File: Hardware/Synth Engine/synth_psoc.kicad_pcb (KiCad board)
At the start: 2 copper layers, 230 parts, among them J1 Barrel_Jack, J10 Conn_01x13, J11 Conn_01x13, J12 Conn_01x06, J13 Conn_01x05, J14 Conn_01x05, J15 Conn_01x05, J16 Conn_01x05, J2 Audio-Jack-2_Switch, J3 SWD_programming, J4 Conn_01x08, J5 Conn_01x02, J6 Conn_01x03, J7 Capsense_buttons, J8 Conn_01x13, J9 Conn_01x13, Q1 MMBT3904-TP, Q2 MMBT3904-TP, Q3 MMBT3904-TP, Q4 MMBT3904-TP, Q5 MMBFJ177, Q6 MMBFJ177, Q7 MMBFJ177, Q8 MMBFJ177, U1 TL074, U2 TL074, U3 TL074, U4 TL074, U5 TL074, U6 CY8C4246AZI-L445, U7 V7805-1000, U8 PT2399, Y1 Crystal

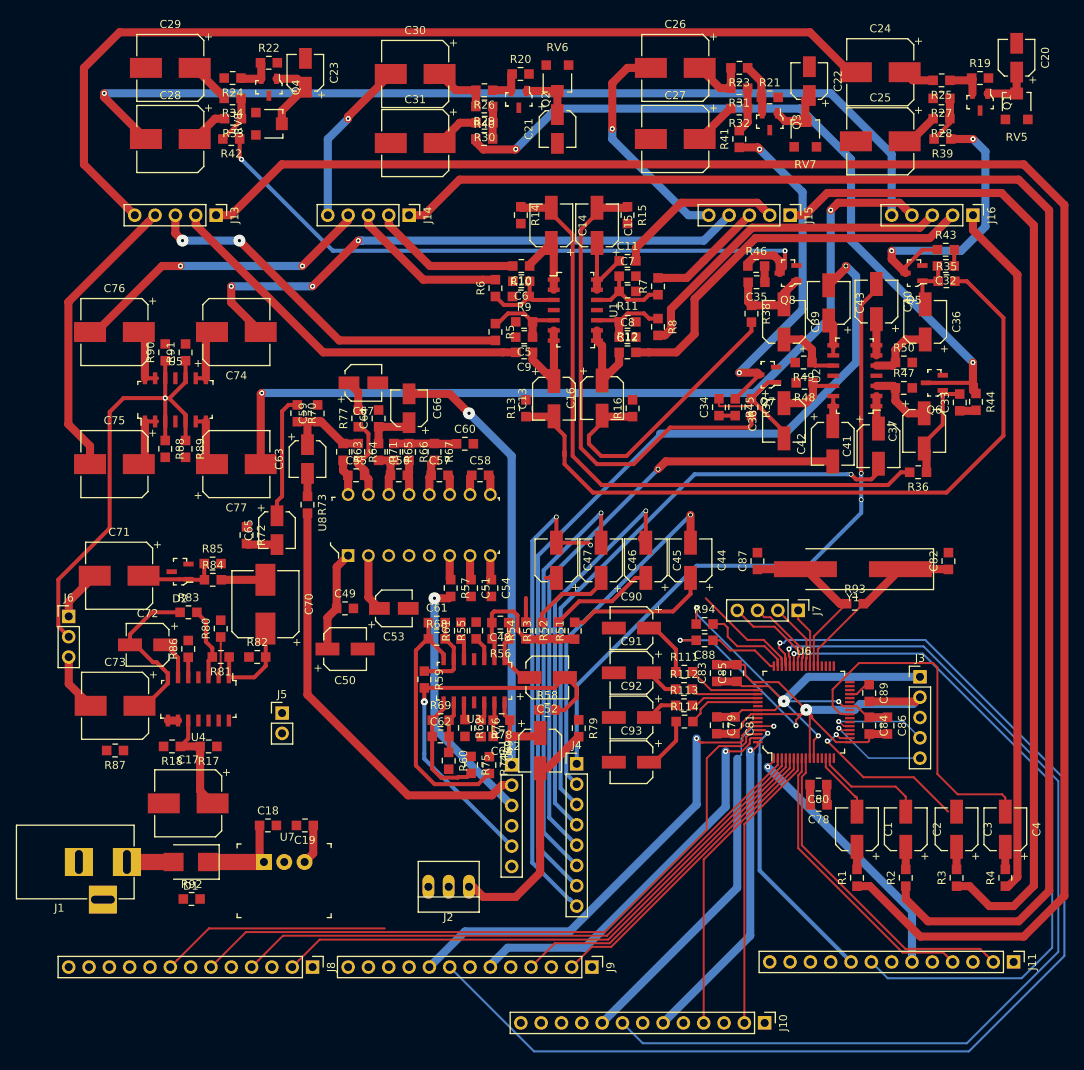
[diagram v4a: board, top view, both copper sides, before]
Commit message: finish routing connectors and start routing +15V
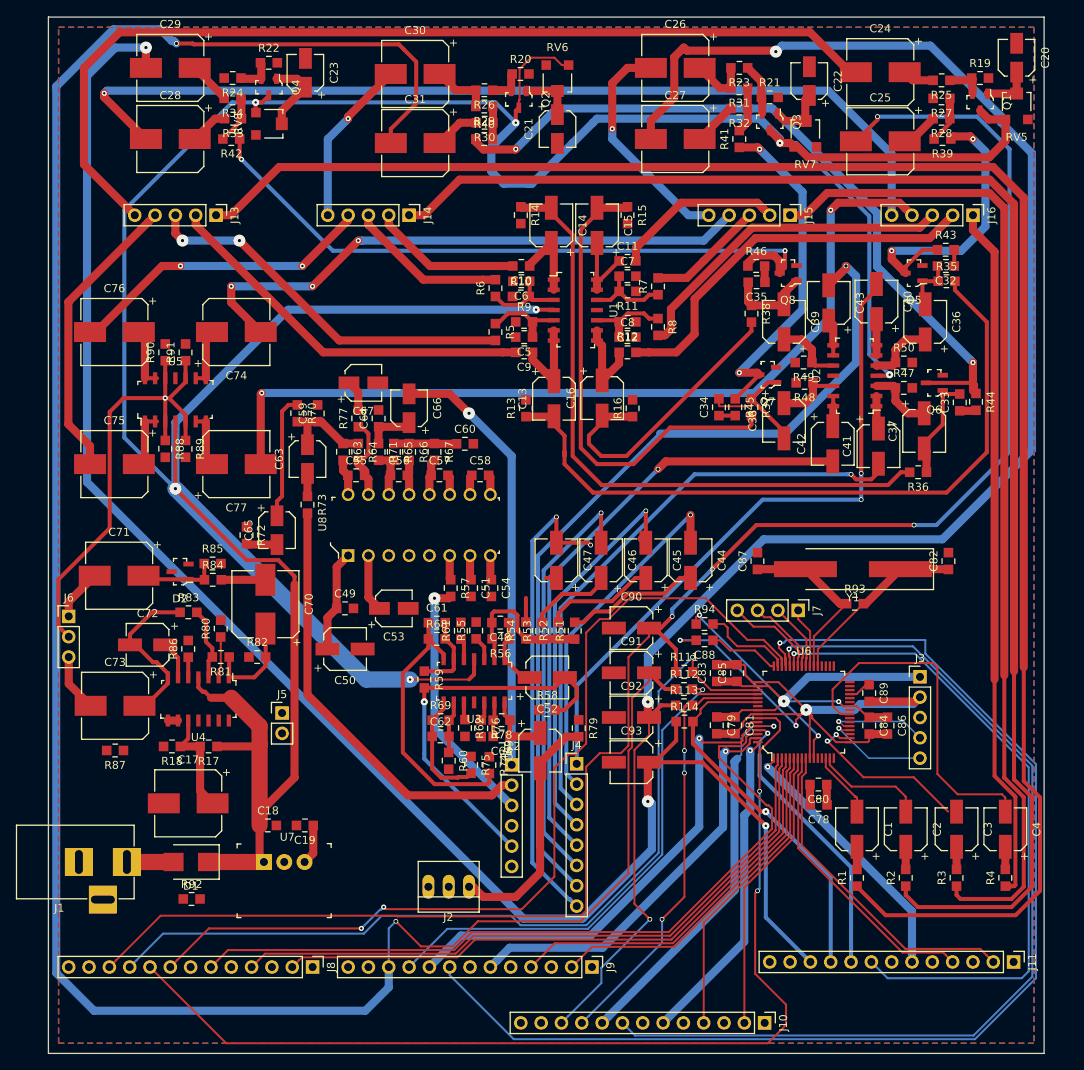
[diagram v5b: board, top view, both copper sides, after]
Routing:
- net +15V: track 11.8 -> 447.2 mm, vias 0 -> 7
- net /Microcontroller/envelope_pwm_2: track 4.16 -> 289.7 mm, vias 0 -> 2
- net /Microcontroller/envelope_pwm_1: track 7.26 -> 224.9 mm, vias 0 -> 4
- net /Microcontroller/envelope_pwm_3: track 3.95 -> 215.0 mm, vias 0 -> 3
- net /Microcontroller/envelope_pwm_4: track 6.89 -> 214.4 mm, vias 0 -> 3
- net /Connectors/osc1_quant: track 0.00 -> 128.1 mm, vias 0 -> 2
- net /Connectors/envelope_pwm_bypass_in_1: track 9.09 -> 110.2 mm, vias 0 -> 1
- net /Connectors/osc1_repeat: track 42.4 -> 115.9 mm, vias 0 -> 2
- net /Connectors/envelope_pwm_bypass_in_2: track 8.44 -> 69.9 mm, vias 0 -> 1
- net /Connectors/envelope_pwm_bypass_in_3: track 8.55 -> 54.5 mm, vias 0 -> 3
- net /Connectors/envelope_pwm_bypass_in_4: track 9.45 -> 47.0 mm, vias 0 -> 1
- net /Connectors/osc1_speed: track 86.0 -> 96.4 mm
- net /Connectors/freq_in_1: track 227.8 -> 218.2 mm
- net /Connectors/freq_in_2: track 190.8 -> 183.5 mm
- net /Connectors/osc2_pwm_wiper: track 43.3 -> 48.0 mm
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- added copper zone on B.Cu, net GND
- added copper zone on F.Cu, net GND
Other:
- board outline added: 124.5 x 129.5 mm

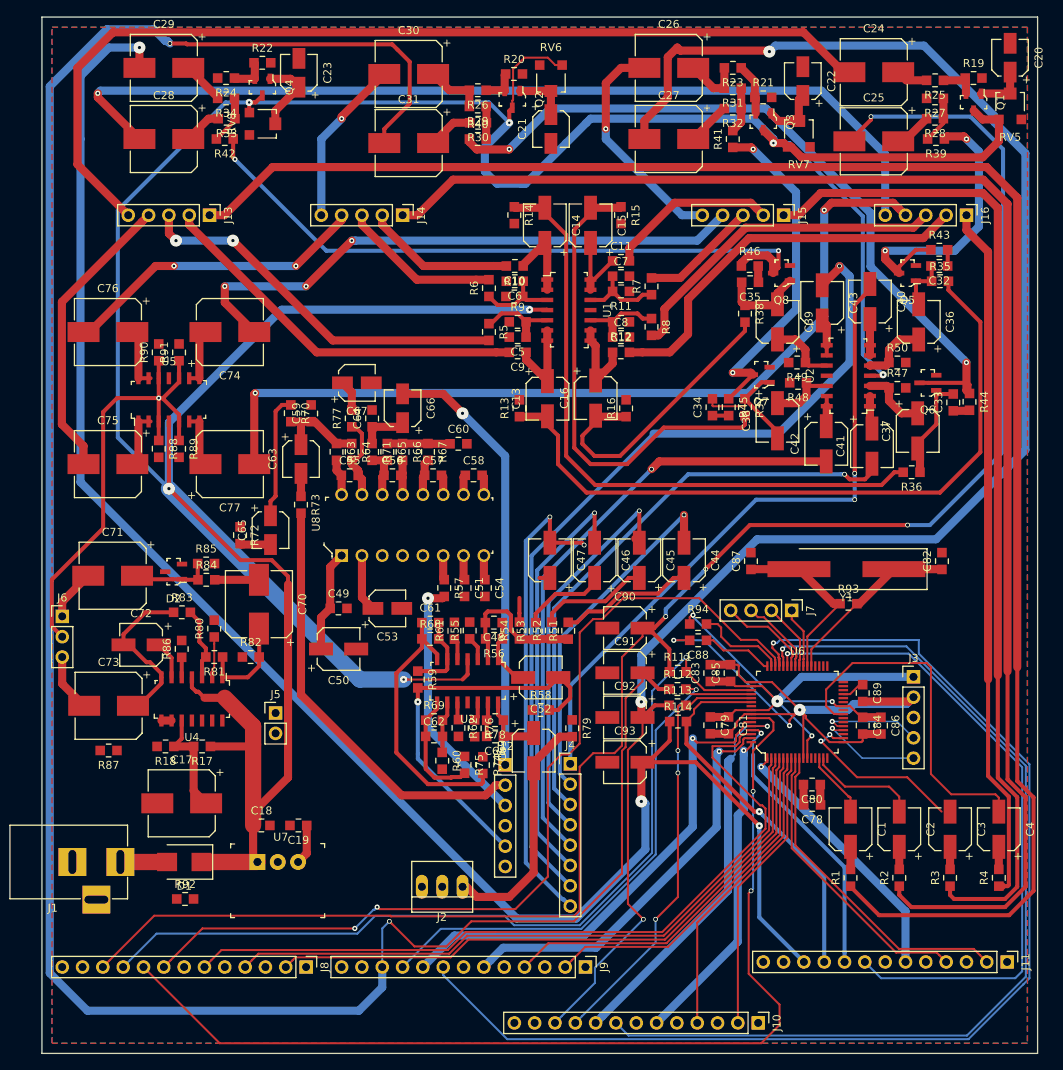
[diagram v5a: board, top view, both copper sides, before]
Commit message: PCBv2 release candidate. Passes DRC.
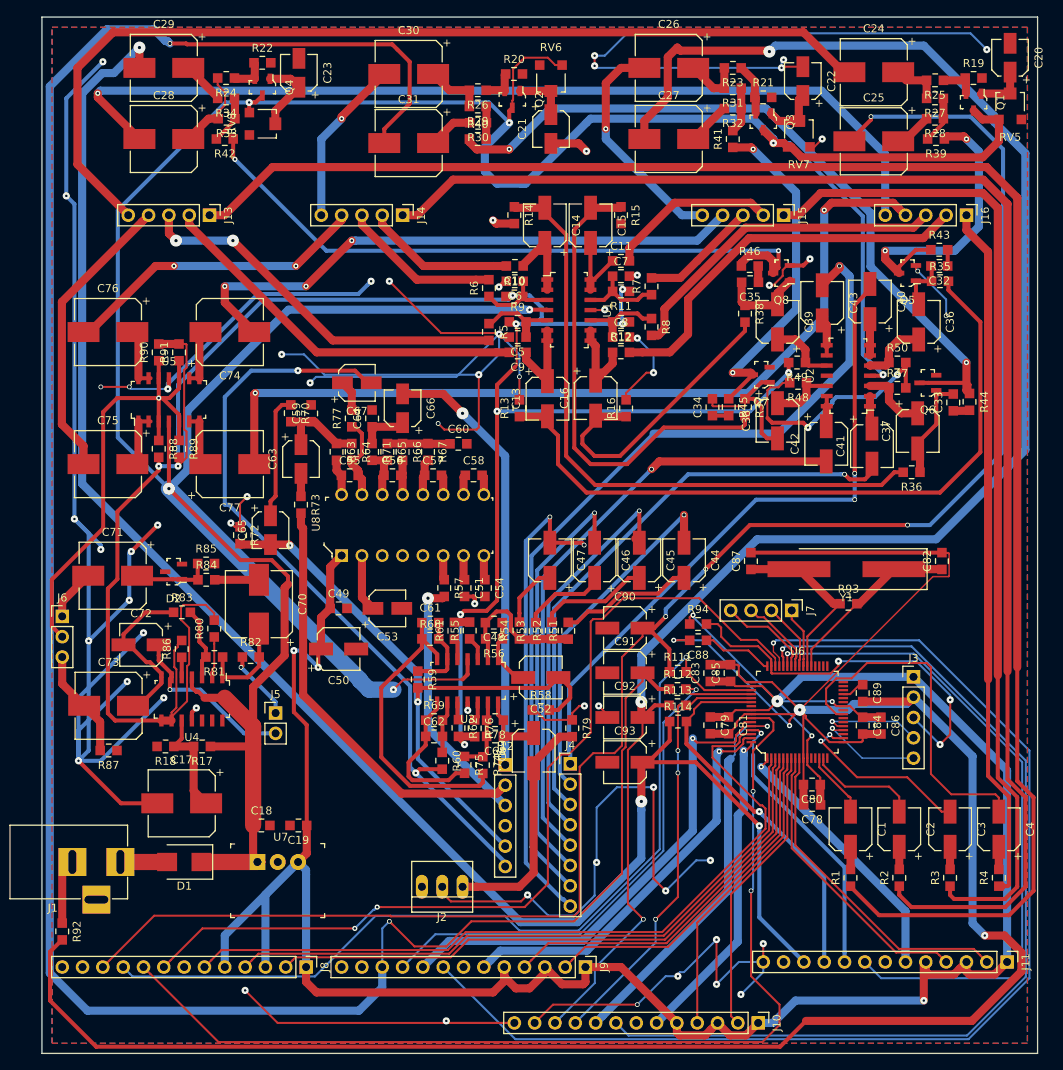
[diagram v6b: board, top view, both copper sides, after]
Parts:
- moved R92 15.9 mm to (2.54, 160.0), turned to 270 degrees
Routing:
- net GND: track 0.00 -> 614.0 mm, vias 0 -> 60
- net VREF: track 1.27 -> 322.3 mm, vias 0 -> 12
- net GNDD: track 93.9 -> 328.6 mm, vias 3 -> 4
- net +5V: track 96.7 -> 330.0 mm, vias 4 -> 7
- net /Mixer and Effects/delay_out: track 0.00 -> 97.3 mm, vias 0 -> 2
- net /Microcontroller/XRES: track 12.3 -> 49.7 mm, vias 0 -> 3
- net /Mixer and Effects/delay_in: track 52.8 -> 81.5 mm, vias 1 -> 2
- net /LFO Modulation and Routing/LFO_freq_out: track 4.73 -> 21.8 mm, vias 0 -> 1
- net /LFO Modulation and Routing/LFO_freq_in: track 0.00 -> 8.86 mm, vias 0 -> 1
- net /LFO Modulation and Routing/lfo_tri: track 7.23 -> 13.6 mm
- net Net-(C28-Pad1): track 4.79 -> 10.6 mm
- net Net-(C68-Pad2): track 4.32 -> 9.36 mm
- net Net-(C62-Pad1): track 14.4 -> 18.3 mm
- net Net-(C47-Pad1): track 4.33 -> 7.86 mm
- net Net-(C61-Pad1): track 34.5 -> 37.8 mm
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
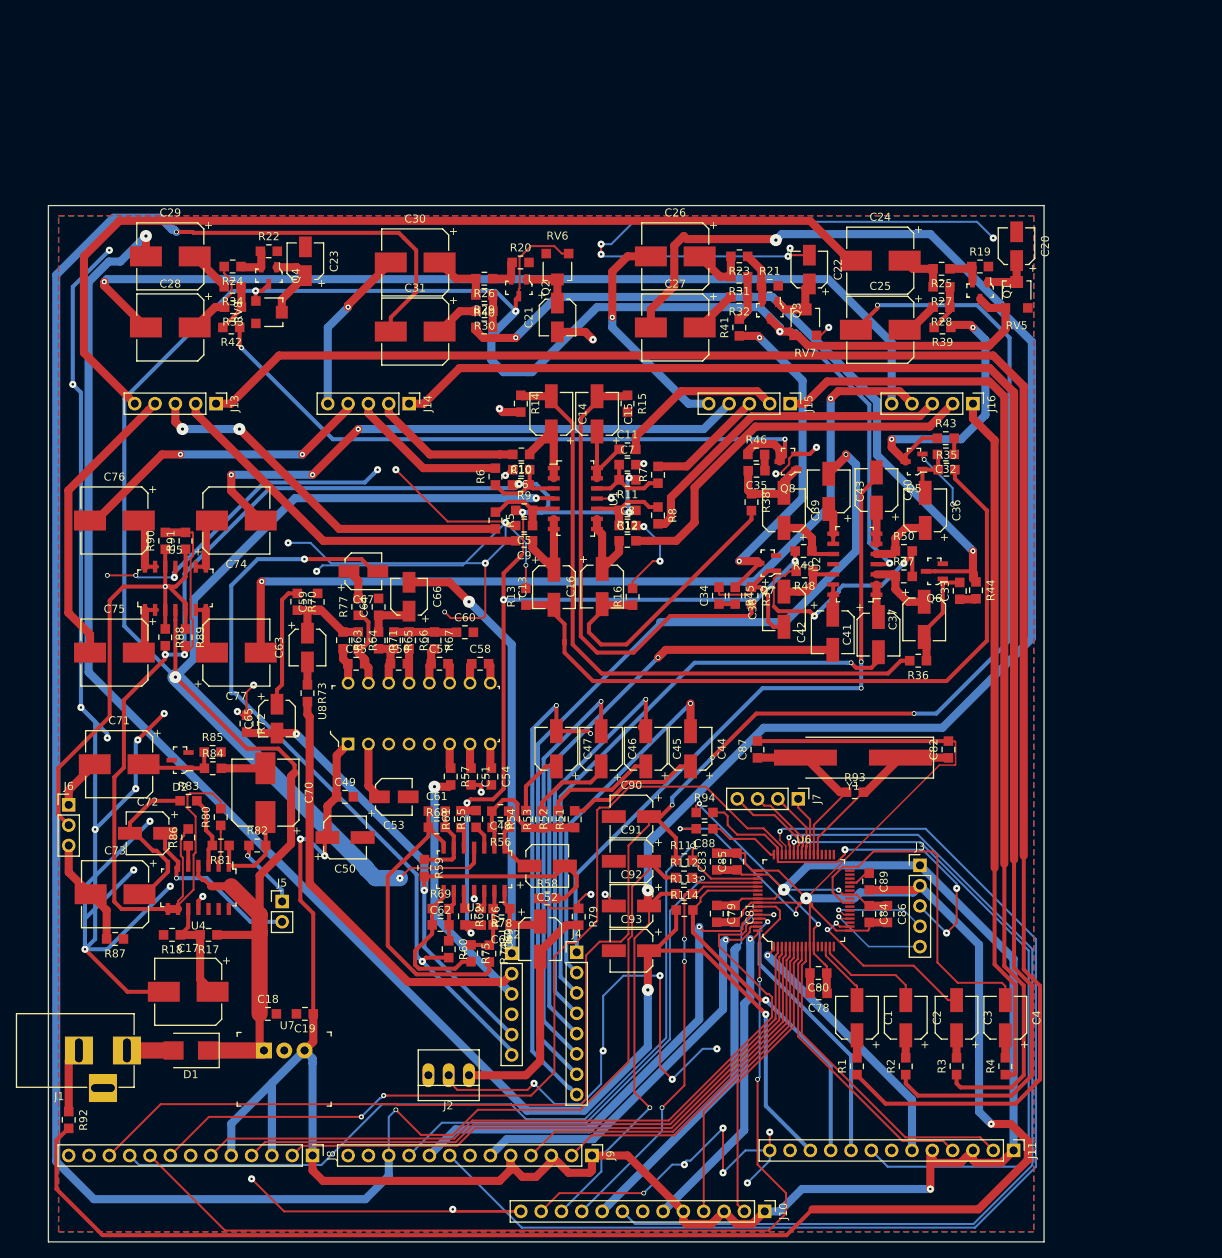
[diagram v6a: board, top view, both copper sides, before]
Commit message: move main synth board so that connector dimensions match between boards.
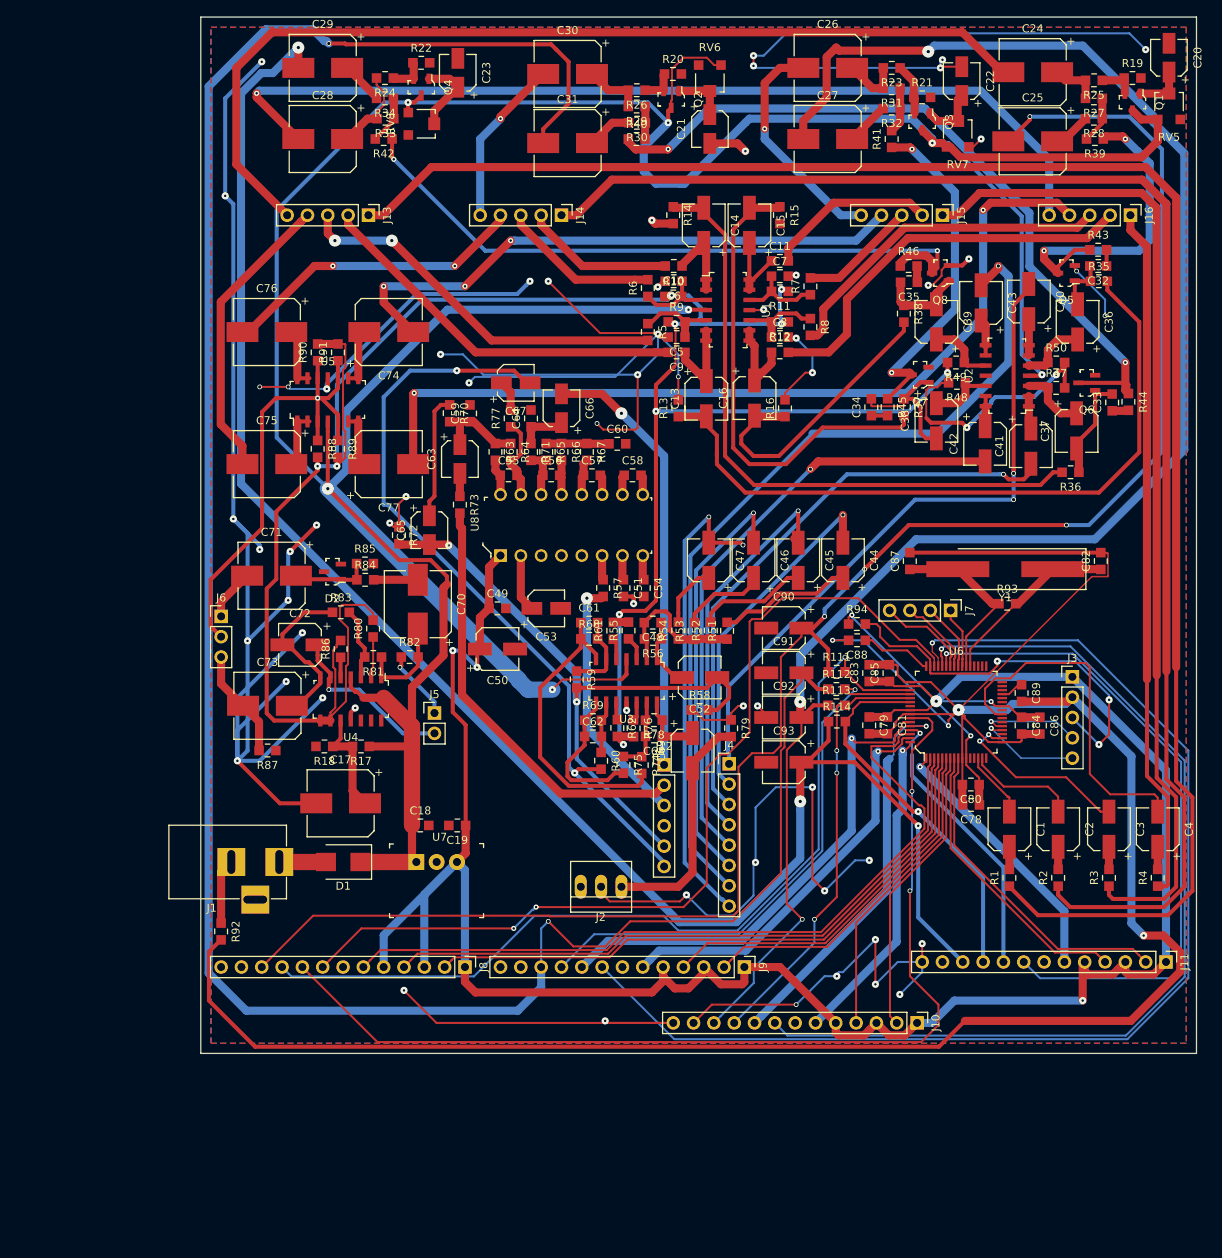
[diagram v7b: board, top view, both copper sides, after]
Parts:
- moved J16 30.7 mm to (135.3, 46.9)
- moved C38 30.3 mm to (111.0, 72.6)
- moved C85 30.3 mm to (105.1, 104.2)
- moved C90 30.3 mm to (91.9, 98.5)
- moved C93 30.3 mm to (91.9, 115.3)
- moved J3 30.3 mm to (128.0, 104.6)
- moved J9 30.3 mm to (87.0, 140.9)
- moved R44 30.3 mm to (135.0, 70.3)
- moved C19 30.3 mm to (51.1, 123.2)
- moved C48 30.3 mm to (75.5, 97.9)
- moved C60 30.3 mm to (71.1, 75.5)
- moved C63 30.3 mm to (51.4, 77.4)
- moved C64 30.3 mm to (60.3, 72.3)
- moved J12 30.3 mm to (77.0, 115.6)
- moved R52 30.3 mm to (82.8, 98.8)
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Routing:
- net Net-(Q5-Pad3): track 36.8 -> 39.9 mm
- net /Connectors/freq_out_4: track 42.0 -> 42.6 mm
- net /lfo_in_4: track 108.5 -> 109.2 mm
- net /Connectors/freq_fb_4: track 49.3 -> 49.9 mm

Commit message: fix remaining connector placement. Routing still WIP
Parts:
- removed J12: Conn_01x06, Pin_Headers:Pin_Header_Straight_1x06_Pitch2.54mm
- J5: value Conn_01x02 -> Conn_01x08; footprint Pin_Headers:Pin_Header_Straight_1x02_Pitch2.54mm -> Pin_Headers:Pin_Header_Straight_1x08_Pitch2.54mm
- moved J6 68.5 mm to (80.9, 131.4), turned to 90 degrees
- moved J5 24.9 mm to (72.4, 115.4)
- moved J4 9.72 mm to (94.8, 115.5)
- moved J2 7.50 mm to (64.6, 128.1)
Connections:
- C72 pad 1: /LFO Modulation and Routing/LFO_freq_out -> /lfo_freq_out
- J5 pad 1: /LFO Modulation and Routing/LFO_freq_in -> /Mixer and Effects/delay_fb_ctrl_in
- J5 pad 2: /LFO Modulation and Routing/LFO_freq_out -> /Mixer and Effects/delay_fb_ctrl_out
- R82 pad 1: /LFO Modulation and Routing/LFO_freq_in -> /lfo_freq_in
- U4 pad 6: /LFO Modulation and Routing/LFO_freq_out -> /lfo_freq_out
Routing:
- net /lfo_freq_out: track 0.00 -> 21.8 mm, vias 0 -> 1
- net /LFO Modulation and Routing/LFO_freq_out: track 21.8 -> 0.00 mm, vias 1 -> 0
- net /lfo_freq_in: track 0.00 -> 8.86 mm, vias 0 -> 1
- net /LFO Modulation and Routing/LFO_freq_in: track 8.86 -> 0.00 mm, vias 1 -> 0
